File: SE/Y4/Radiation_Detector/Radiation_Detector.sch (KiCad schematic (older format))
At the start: 14 parts, among them J1 Bus

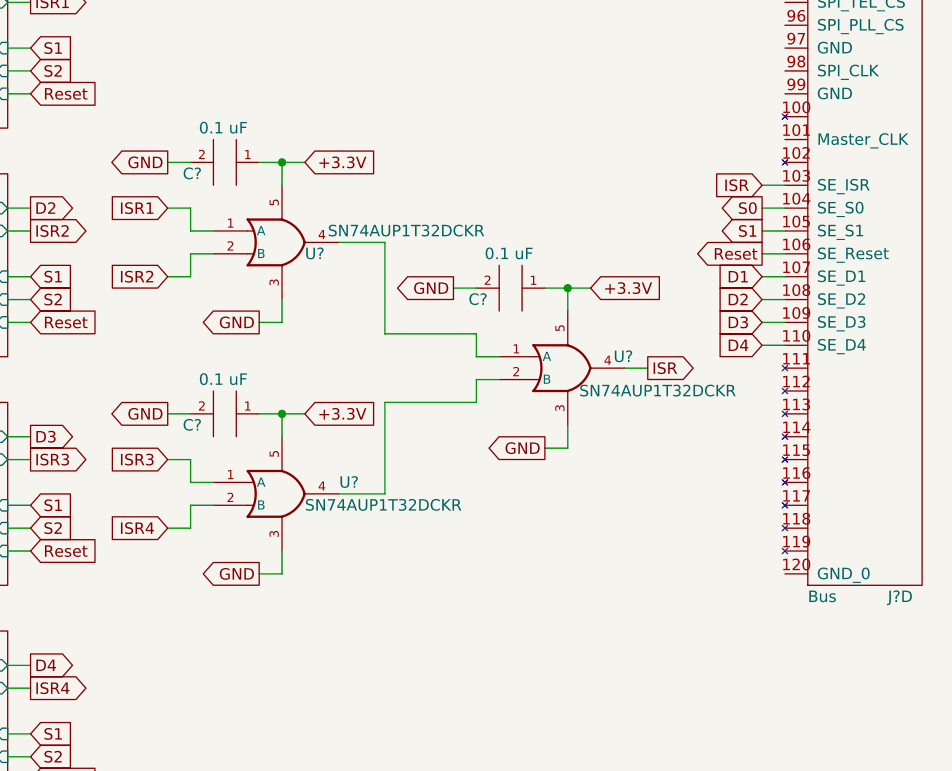
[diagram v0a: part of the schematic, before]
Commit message: SiPM schematic symbol modified
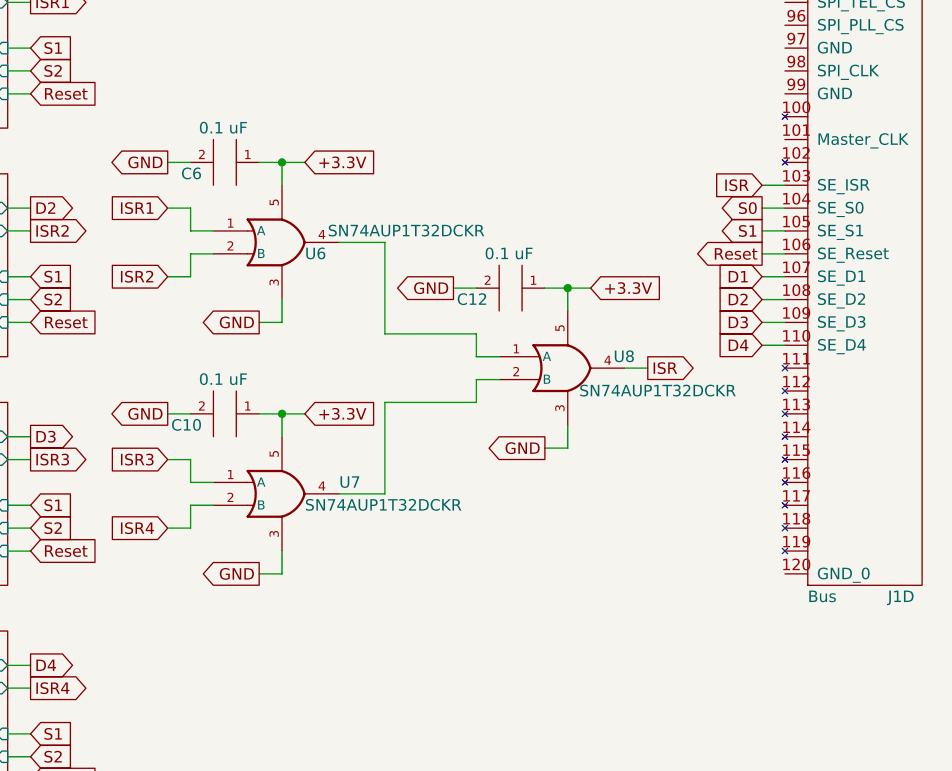
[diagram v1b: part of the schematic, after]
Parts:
- gave numbers to parts that had none: 7
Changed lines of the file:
@@
 +5V
 $Comp
-L power:+5V #PWR?
+L power:+5V #PWR0101
 U 1 1 5EC3D995
 P 1350 3050
-F 0 "#PWR?" H 1350 2900 50  0001 C CNN
+F 0 "#PWR0101" H 1350 2900 50  0001 C CNN
 F 1 "+5V" H 1450 3150 50  0000 C CNN
 F 2 "" H 1350 3050 50  0001 C CNN
@@
 	1150 2650 1350 2650
 $Comp
-L power:+36V #PWR?
+L power:+36V #PWR0102
 U 1 1 5EC3F7A4
 P 1350 2650
-F 0 "#PWR?" H 1350 2500 50  0001 C CNN
+F 0 "#PWR0102" H 1350 2500 50  0001 C CNN
 F 1 "+36V" H 1450 2750 50  0000 C CNN
 F 2 "" H 1350 2650 50  0001 C CNN
@@
 +3.3V
 $Comp
-L power:+3V3 #PWR?
+L power:+3V3 #PWR0103
 U 1 1 5EF0B44D
 P 1350 3250
-F 0 "#PWR?" H 1350 3100 50  0001 C CNN
+F 0 "#PWR0103" H 1350 3100 50  0001 C CNN
 F 1 "+3V3" H 1450 3350 50  0000 C CNN
 F 2 "" H 1350 3250 50  0001 C CNN
@@
 	5700 4000 6100 4000
 $Comp
-L SS:Bus J?
+L SS:Bus J1
 U 4 1 5EC7146A
 P 10600 2000
-F 0 "J?" V 12150 2450 50  0000 L CNN
+F 0 "J1" V 12150 2450 50  0000 L CNN
 F 1 "Bus" V 12150 2100 50  0000 L CNN
 F 2 "" H 9300 2700 50  0001 C CNN
@@
 AR Path="/5EC6BD52/5EC879CD" Ref="U?"  Part="1"
 AR Path="/5EC6D692/5EC879CD" Ref="U?"  Part="1"
-AR Path="/5EC879CD" Ref="U?"  Part="1"
-F 0 "U?" H 8500 1750 50  0000 L CNN
+AR Path="/5EC879CD" Ref="U6"  Part="1"
+F 0 "U6" H 8500 1750 50  0000 L CNN
 F 1 "SN74AUP1T32DCKR" H 8600 1850 50  0000 L CNN
 F 2 "" H 8200 2150 50  0001 C CNN
@@
 $EndComp
 $Comp
-L 001:C C?
+L 001:C C6
 U 1 1 5EC879D4
 P 8300 1650
-AR Path="/5EC879D4" Ref="C?"  Part="1"
+AR Path="/5EC879D4" Ref="C6"  Part="1"
 AR Path="/5EBDE6C5/5EC879D4" Ref="C?"  Part="1"
 AR Path="/5EEC35BD/5EC879D4" Ref="C?"  Part="1"
@@
 AR Path="/5EC6BD52/5EC879D4" Ref="C?"  Part="1"
 AR Path="/5EC6D692/5EC879D4" Ref="C?"  Part="1"
-F 0 "C?" H 8550 1700 50  0000 L CNN
+F 0 "C6" H 8550 1700 50  0000 L CNN
 F 1 "0.1 uF" H 8350 1500 50  0000 L CNN
 F 2 "" H 8350 1740 50  0001 C CNN
@@
 AR Path="/5EC6BD52/5EC879ED" Ref="U?"  Part="1"
 AR Path="/5EC6D692/5EC879ED" Ref="U?"  Part="1"
-AR Path="/5EC879ED" Ref="U?"  Part="1"
-F 0 "U?" H 8650 2950 50  0000 L CNN
+AR Path="/5EC879ED" Ref="U7"  Part="1"
+F 0 "U7" H 8650 2950 50  0000 L CNN
 F 1 "SN74AUP1T32DCKR" H 8500 2850 50  0000 L CNN
 F 2 "" H 8200 3250 50  0001 C CNN
@@
 $EndComp
 $Comp
-L 001:C C?
+L 001:C C10
 U 1 1 5EC879F4
 P 8300 2750
-AR Path="/5EC879F4" Ref="C?"  Part="1"
+AR Path="/5EC879F4" Ref="C10"  Part="1"
 AR Path="/5EBDE6C5/5EC879F4" Ref="C?"  Part="1"
 AR Path="/5EEC35BD/5EC879F4" Ref="C?"  Part="1"
@@
 AR Path="/5EC6BD52/5EC879F4" Ref="C?"  Part="1"
 AR Path="/5EC6D692/5EC879F4" Ref="C?"  Part="1"
-F 0 "C?" H 8550 2800 50  0000 L CNN
+F 0 "C10" H 8550 2800 50  0000 L CNN
 F 1 "0.1 uF" H 8350 2600 50  0000 L CNN
 F 2 "" H 8350 2840 50  0001 C CNN
@@
 AR Path="/5EC6BD52/5EC87A0D" Ref="U?"  Part="1"
 AR Path="/5EC6D692/5EC87A0D" Ref="U?"  Part="1"
-AR Path="/5EC87A0D" Ref="U?"  Part="1"
-F 0 "U?" H 9850 2400 50  0000 L CNN
+AR Path="/5EC87A0D" Ref="U8"  Part="1"
+F 0 "U8" H 9850 2400 50  0000 L CNN
 F 1 "SN74AUP1T32DCKR" H 9700 2250 50  0000 L CNN
 F 2 "" H 9450 2700 50  0001 C CNN
@@
 $EndComp
 $Comp
-L 001:C C?
+L 001:C C12
 U 1 1 5EC87A14
 P 9550 2200
-AR Path="/5EC87A14" Ref="C?"  Part="1"
+AR Path="/5EC87A14" Ref="C12"  Part="1"
 AR Path="/5EBDE6C5/5EC87A14" Ref="C?"  Part="1"
 AR Path="/5EEC35BD/5EC87A14" Ref="C?"  Part="1"
@@
 AR Path="/5EC6BD52/5EC87A14" Ref="C?"  Part="1"
 AR Path="/5EC6D692/5EC87A14" Ref="C?"  Part="1"
-F 0 "C?" H 9800 2250 50  0000 L CNN
+F 0 "C12" H 9800 2250 50  0000 L CNN
 F 1 "0.1 uF" H 9600 2050 50  0000 L CNN
 F 2 "" H 9600 2290 50  0001 C CNN

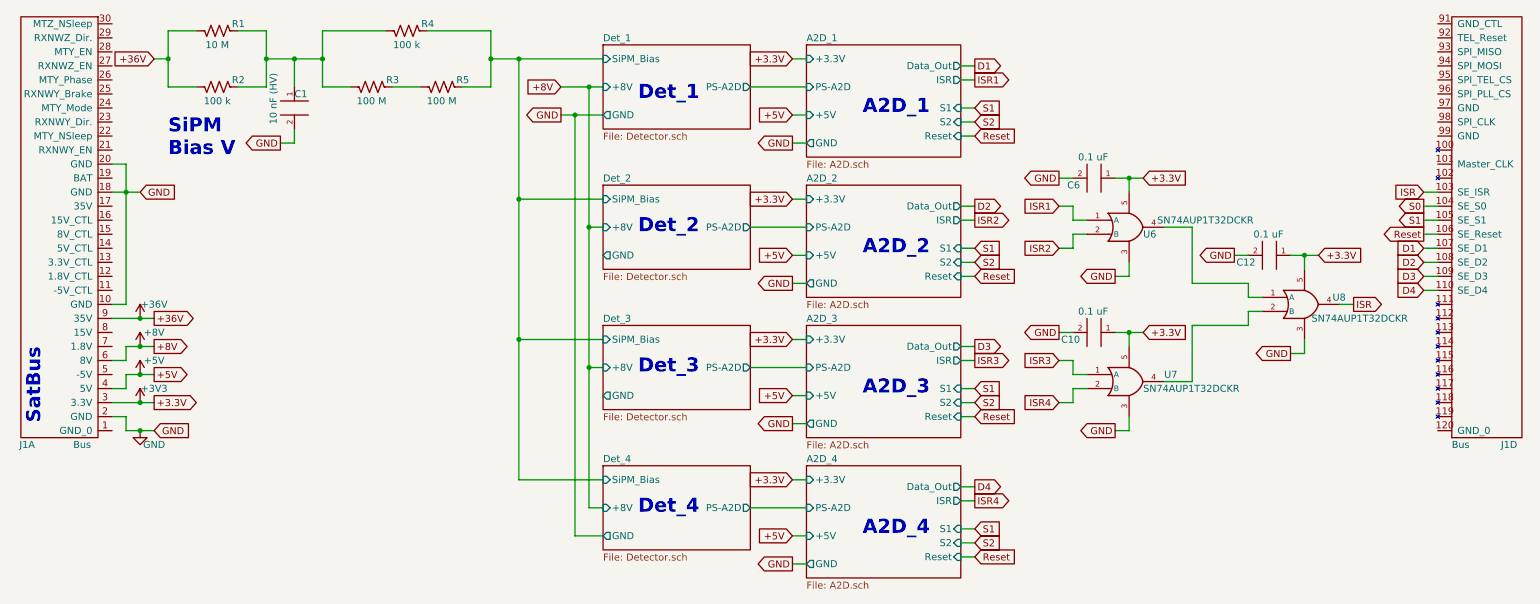
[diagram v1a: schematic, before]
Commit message: cleaned up schematic and clarified
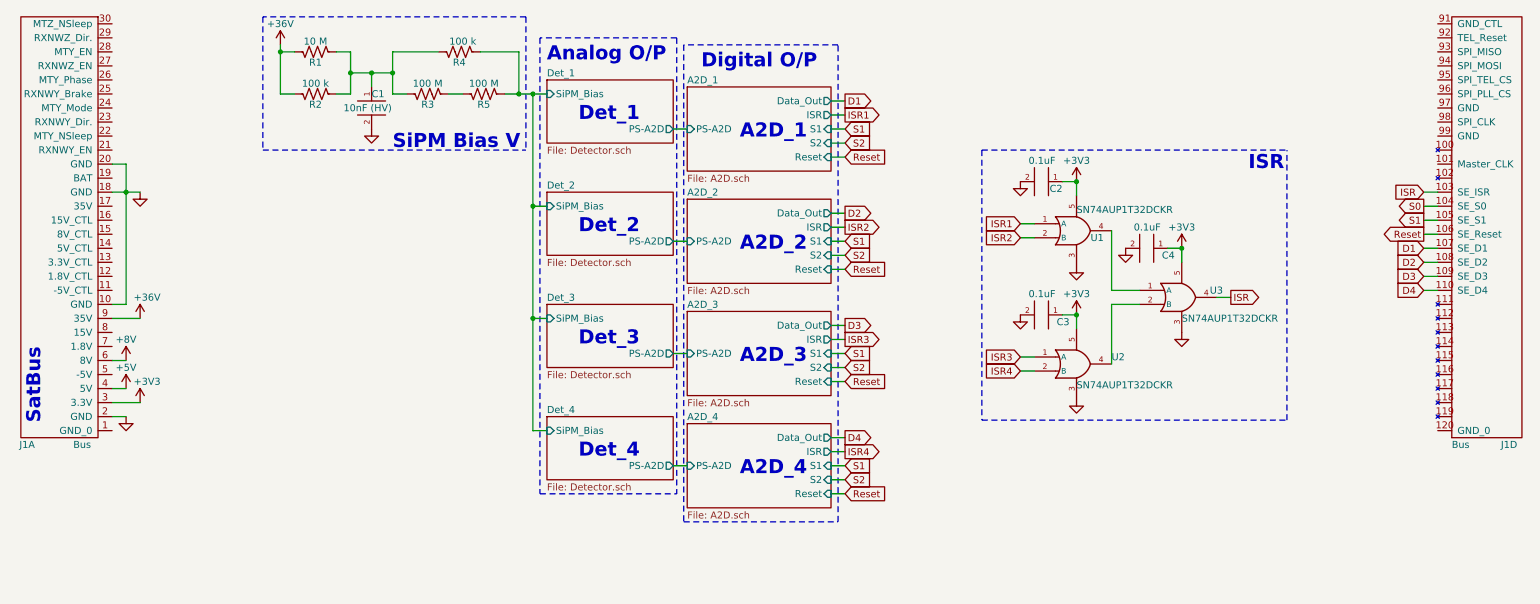
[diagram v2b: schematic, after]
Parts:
- C1: value 10 nF (HV) -> 10nF (HV)
- C2: renamed from C6; value 0.1 uF -> 0.1uF
- C3: renamed from C10; value 0.1 uF -> 0.1uF
- C4: renamed from C12; value 0.1 uF -> 0.1uF
- renumbered U6 to U1, U7 to U2, U8 to U3
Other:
- note added: "Analog O/P\n"
- note added: "Det_2\n"
- note added: "Det_4"
- note added: "Digital O/P\n"
- note added: "ISR"
- note added: "SiPM Bias V"
- note removed: "Det_2"
- note removed: "Det_4\n"
- note removed: "SiPM\nBias V"
- moved on the sheet: C1, C2, C3, C4, R1, R2, R3, R4, R5, U1, U2, U3

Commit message: updated schematic labeling
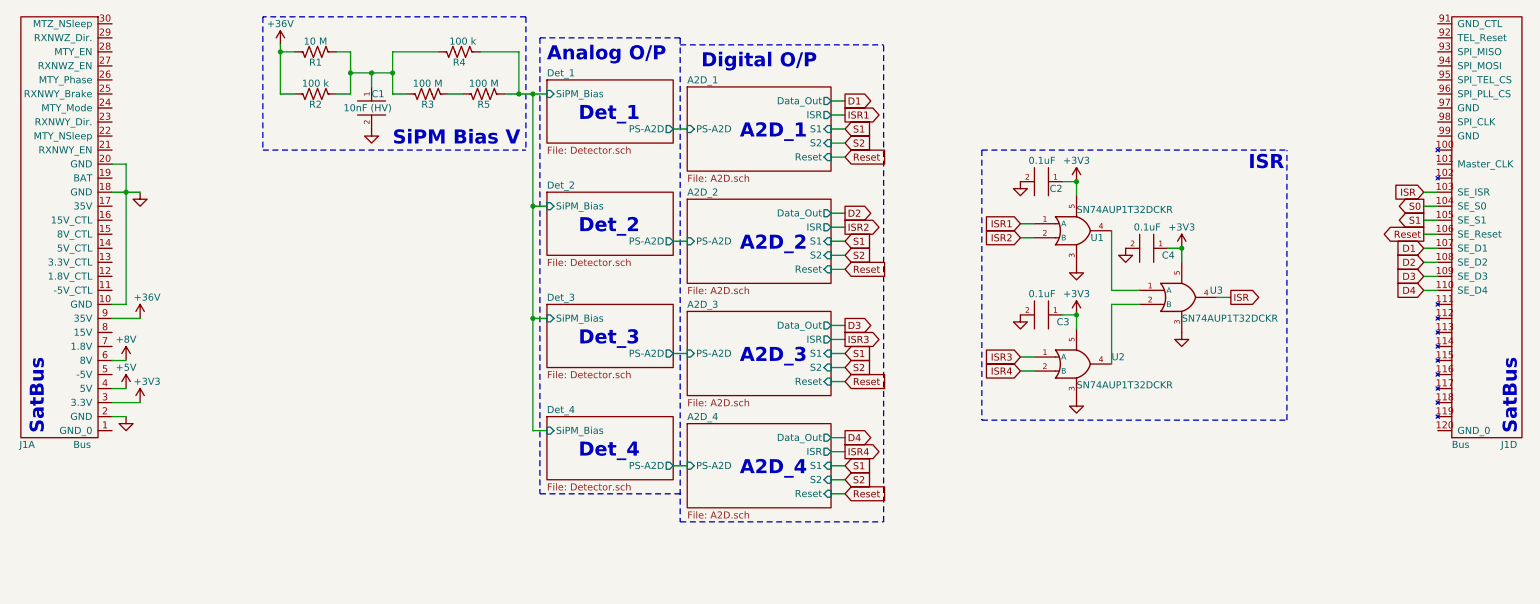
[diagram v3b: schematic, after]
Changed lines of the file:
@@
 Wire Wire Line
 	1250 1750 1250 1550
-Text Notes 650  3400 1    100  ~ 20
+Text Notes 675  3475 1    100  ~ 20
 SatBus
-Text Notes 3150 1450 0    100  ~ 20
+Text Notes 3150 1425 0    100  ~ 20
 SiPM Bias V
 $Sheet
@@
 	4100 500  4100 1450
 Wire Notes Line
-	5175 650  4200 650
-Wire Notes Line
-	4200 3900 5175 3900
+	5200 650  4200 650
 Text Notes 4250 825  0    100  ~ 20
 Analog O/P\n
 Wire Notes Line
-	5175 650  5175 3900
-Wire Notes Line
 	4200 650  4200 3900
 Wire Notes Line
-	5225 4100 6325 4100
-Wire Notes Line
-	6325 4100 6325 700
-Wire Notes Line
-	6325 700  5225 700
+	6650 4100 6650 700
 Text Notes 5350 875  0    100  ~ 20
 Digital O/P\n
-Wire Notes Line
-	5225 700  5225 4100
 $Comp
 L SS:SN74AUP1T32DCKR U?
@@
 Text Notes 9250 1600 0    100  ~ 20
 ISR
+Wire Notes Line
+	4200 3900 5200 3900
+Wire Notes Line
+	5200 650  5200 4100
+Wire Notes Line
+	5200 700  6650 700
+Wire Notes Line
+	5200 4100 6650 4100
+Text Notes 11175 3475 1    100  ~ 20
+SatBus
 $EndSCHEMATC

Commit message: SE is donezo for Y4
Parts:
- removed C1: 10nF (HV), symbol 001:C
- removed C2, C3, C4: 0.1uF, symbol 001:C
- removed R1: 10 M, symbol Device:R_US
- removed R2, R4: 100 k, symbol Device:R_US
- removed R3, R5: 100 M, symbol Device:R_US
- removed U1, U2, U3: SN74AUP1T32DCKR, symbol SS:SN74AUP1T32DCKR
- added C?: 10nF (HV), symbol Device:C_Small
- added C?: 1uF, symbol Device:CP1_Small
- added C?: 10nF, symbol Device:C_Small
- added C?: 0.1 uF, symbol Device:C_Small
- added R?: 10M, symbol Device:R_Small_US
- added R? (x2): 100k, symbol Device:R_Small_US
- added R? (x2): 100M, symbol Device:R_Small_US
- added U?: 74AUP1G04, symbol SS:74AUP1G04
- J1: symbol SS:Bus -> Radiation_Detector-rescue:Bus-SS
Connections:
- net ISR is gone; now on net D3: J1.103 (SE_D03)
- net S0 is gone; now on net D4: J1.104 (SE_D04)
- net +36V: now also R?.2, R?.2
- net +3V3: now also C?.1, C?.2, C?.2, U?.4 (VCC)
- net D1: now also J1.101 (SE_D01); no longer J1.107 (SE_D1)
- net D2: now also J1.102 (SE_D02); no longer J1.108 (SE_D2)
- net D3: no longer J1.109 (SE_D3)
- net D4: no longer J1.110 (SE_D4)
- net Det_1/SiPM_Bias: now also R?.1, R?.1
- net GND: now also J1.117 (GND), J1.95 (GND~), C?.1, C?.1, C?.1, C?.2, U?.2 (GND)
- net ISR1: now also J1.96 (SE_ISR1~)
- net ISR2: now also J1.97 (SE_ISR2)
- net ISR3: now also J1.98 (SE_ISR3~)
- net ISR4: now also J1.99 (SE_ISR4)
- net Reset: now also J1.116 (SE_FF_CLR~), U?.1 (A); no longer J1.106 (SE_Reset)
- net -5V: now reaches J1.5 (-5V)
- net D0: now reaches J1.100 (SE_D00)
- net D11: now reaches J1.111 (SE_D11)
- net D12: now reaches J1.112 (SE_D12)
- net D13: now reaches J1.113 (SE_D13)
- net D14: now reaches J1.114 (SE_D14)
- net D15: now reaches J1.115 (SE_D15)
- net +8V: no longer names the net of J1.6 (8V)
- net S1 renamed D5
- new net: C?.2, R?.1, R?.1, R?.2, R?.2
- new net: R?.1, R?.2
- new net CLR: U?.3 (Y)
- new net D10: J1.110 (SE_D10)
- new net D6: J1.106 (SE_D06)
- new net D7: J1.107 (SE_D07)
- new net D8: J1.108 (SE_D08)
- new net D9: J1.109 (SE_D09)
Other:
- note added: "Analog\n"
- note added: "Digital"
- note added: "RESET"
- note added: "SiPM Bias"
- note removed: "Analog O/P\n"
- note removed: "Digital O/P\n"
- note removed: "ISR"
- note removed: "SiPM Bias V"
- moved on the sheet: J1A
